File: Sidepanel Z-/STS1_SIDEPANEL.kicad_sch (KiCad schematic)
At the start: 7 parts, among them J1 Conn_01x18, J3 Conn_01x12

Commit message: moved the connectors, changed the footprint of the input and output capacitors and splitted the input capacitor in two
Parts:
- UV1: footprint STS_connector:5014610491 -> STS_connector:200528-0040
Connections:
- net at cam1.1: now also edu_con1.22; no longer edu_con1.1
- net at cam1.10: now also edu_con1.13; no longer edu_con1.10
- net at cam1.11: now also edu_con1.12; no longer edu_con1.11
- net at cam1.12: now also edu_con1.11; no longer edu_con1.12
- net at cam1.13: now also edu_con1.10; no longer edu_con1.13
- net at cam1.14: now also edu_con1.9; no longer edu_con1.14
- net at cam1.15: now also edu_con1.8; no longer edu_con1.15
- net at cam1.16: now also edu_con1.7; no longer edu_con1.16
- net at cam1.17: now also edu_con1.6; no longer edu_con1.17
- net at cam1.18: now also edu_con1.5; no longer edu_con1.18
- net at cam1.19: now also edu_con1.4; no longer edu_con1.19
- net at cam1.2: now also edu_con1.21; no longer edu_con1.2
- net at cam1.20: now also edu_con1.3; no longer edu_con1.20
- net at cam1.21: now also edu_con1.2; no longer edu_con1.21
- net at cam1.22: now also edu_con1.1; no longer edu_con1.22
- net at cam1.3: now also edu_con1.20; no longer edu_con1.3
- net at cam1.4: now also edu_con1.19; no longer edu_con1.4
- net at cam1.5: now also edu_con1.18; no longer edu_con1.5
- net at cam1.6: now also edu_con1.17; no longer edu_con1.6
- net at cam1.7: now also edu_con1.16; no longer edu_con1.7
- net at cam1.8: now also edu_con1.15; no longer edu_con1.8
- net at cam1.9: now also edu_con1.14; no longer edu_con1.9
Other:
- moved on the sheet: edu_con1
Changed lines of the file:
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@@
   (no_connect (at 132.715 71.755))
   (no_connect (at 40.64 119.38))
-  (no_connect (at 182.245 71.755))
+  (no_connect (at 182.245 122.555))
   (no_connect (at 40.005 109.22))
   (no_connect (at 79.375 78.74))
-  (no_connect (at 182.245 69.215))
+  (no_connect (at 182.245 120.015))
   (no_connect (at 132.715 69.215))
   (no_connect (at 40.005 106.68))
@@
     )
   )
-  (symbol (lib_id "Cam:54548-2271") (at 182.245 69.215 0) (mirror y) (unit 1)
-    (in_bom yes) (on_board yes) (dnp no) (fields_autoplaced)
-    (property "Reference" "edu_con1" (at 170.815 56.515 0)
+  (symbol (lib_id "Cam:54548-2271") (at 182.245 122.555 180) (unit 1)
+    (in_bom yes) (on_board yes) (dnp no)
+    (property "Reference" "edu_con1" (at 170.815 135.255 0)
       (effects (font (size 1.27 1.27)))
     )
-    (property "Value" "54548-2271" (at 170.815 59.055 0)
+    (property "Value" "54548-2271" (at 170.815 132.715 0)
       (effects (font (size 1.27 1.27)))
     )
-    (property "Footprint" "STS_connector:545482271" (at 182.245 69.215 0)
-      (effects (font (size 1.27 1.27)) hide)
-    )
-    (property "Datasheet" "" (at 182.245 69.215 0)
-      (effects (font (size 1.27 1.27)) hide)
-    )
-    (property "Reference_1" "J4" (at 170.815 61.595 0)
+    (property "Footprint" "STS_connector:545482271" (at 182.245 122.555 0)
+      (effects (font (size 1.27 1.27)) hide)
+    )
+    (property "Datasheet" "" (at 182.245 122.555 0)
+      (effects (font (size 1.27 1.27)) hide)
+    )
+    (property "Reference_1" "J4" (at 170.815 130.175 0)
       (effects (font (size 1.27 1.27)))
     )
-    (property "Value_1" "54548-2271" (at 170.815 64.135 0)
-      (effects (font (size 1.27 1.27)) hide)
-    )
-    (property "Footprint_1" "545482271" (at 163.195 164.135 0)
-      (effects (font (size 1.27 1.27)) (justify left top) hide)
-    )
-    (property "Datasheet_1" "http://www.molex.com/webdocs/datasheets/pdf/en-us//0545482271_FFC_FPC_CONNECTORS.pdf" (at 163.195 264.135 0)
-      (effects (font (size 1.27 1.27)) (justify left top) hide)
-    )
-    (property "Height" "1" (at 163.195 464.135 0)
-      (effects (font (size 1.27 1.27)) (justify left top) hide)
-    )
-    (property "Manufacturer_Name" "Molex" (at 163.195 564.135 0)
-      (effects (font (size 1.27 1.27)) (justify left top) hide)
-    )
-    (property "Manufacturer_Part_Number" "54548-2271" (at 163.195 664.135 0)
-      (effects (font (size 1.27 1.27)) (justify left top) hide)
-    )
-    (property "Mouser Part Number" "538-54548-2271" (at 163.195 764.135 0)
-      (effects (font (size 1.27 1.27)) (justify left top) hide)
-    )
-    (property "Mouser Price/Stock" "https://www.mouser.co.uk/ProductDetail/Molex/54548-2271?qs=qM7ngqbhX5X3ZiWzRWv9wA%3D%3D" (at 163.195 864.135 0)
-      (effects (font (size 1.27 1.27)) (justify left top) hide)
-    )
-    (property "Arrow Part Number" "" (at 163.195 964.135 0)
-      (effects (font (size 1.27 1.27)) (justify left top) hide)
-    )
-    (property "Arrow Price/Stock" "" (at 163.195 1064.135 0)
+    (property "Value_1" "54548-2271" (at 170.815 127.635 0)
+      (effects (font (size 1.27 1.27)) hide)
+    )
+    (property "Footprint_1" "545482271" (at 163.195 27.635 0)
+      (effects (font (size 1.27 1.27)) (justify left top) hide)
+    )
+    (property "Datasheet_1" "http://www.molex.com/webdocs/datasheets/pdf/en-us//0545482271_FFC_FPC_CONNECTORS.pdf" (at 163.195 -72.365 0)
+      (effects (font (size 1.27 1.27)) (justify left top) hide)
+    )
+    (property "Height" "1" (at 163.195 -272.365 0)
+      (effects (font (size 1.27 1.27)) (justify left top) hide)
+    )
+    (property "Manufacturer_Name" "Molex" (at 163.195 -372.365 0)
+      (effects (font (size 1.27 1.27)) (justify left top) hide)
+    )
+    (property "Manufacturer_Part_Number" "54548-2271" (at 163.195 -472.365 0)
+      (effects (font (size 1.27 1.27)) (justify left top) hide)
+    )
+    (property "Mouser Part Number" "538-54548-2271" (at 163.195 -572.365 0)
+      (effects (font (size 1.27 1.27)) (justify left top) hide)
+    )
+    (property "Mouser Price/Stock" "https://www.mouser.co.uk/ProductDetail/Molex/54548-2271?qs=qM7ngqbhX5X3ZiWzRWv9wA%3D%3D" (at 163.195 -672.365 0)
+      (effects (font (size 1.27 1.27)) (justify left top) hide)
+    )
+    (property "Arrow Part Number" "" (at 163.195 -772.365 0)
+      (effects (font (size 1.27 1.27)) (justify left top) hide)
+    )
+    (property "Arrow Price/Stock" "" (at 163.195 -872.365 0)
       (effects (font (size 1.27 1.27)) (justify left top) hide)
     )
@@
       (effects (font (size 1.27 1.27)) hide)
     )
-    (property "Footprint" "STS_connector:5014610491" (at 79.375 76.2 0)
-      (effects (font (size 1.27 1.27)) hide)
-    )
+    (property "Footprint" "STS_connector:200528-0040" (at 79.375 76.2 0)
+      (effects (font (size 1.27 1.27)) hide)
+    )

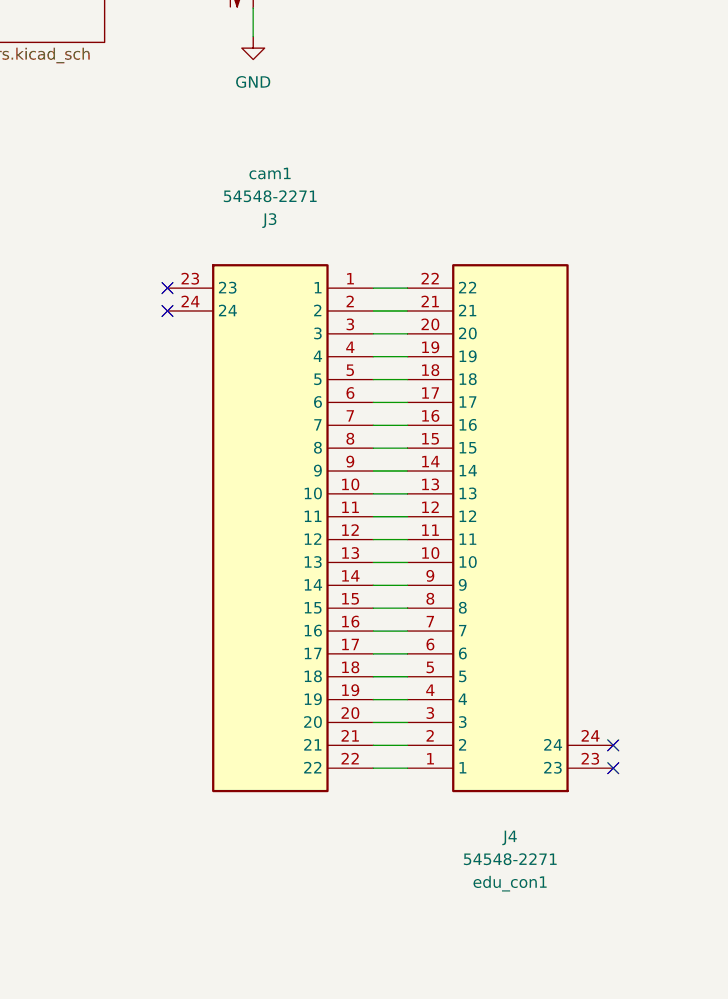
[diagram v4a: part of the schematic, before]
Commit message: Z- Cam Connerctor Rerout, add vias & 90deg trace removal
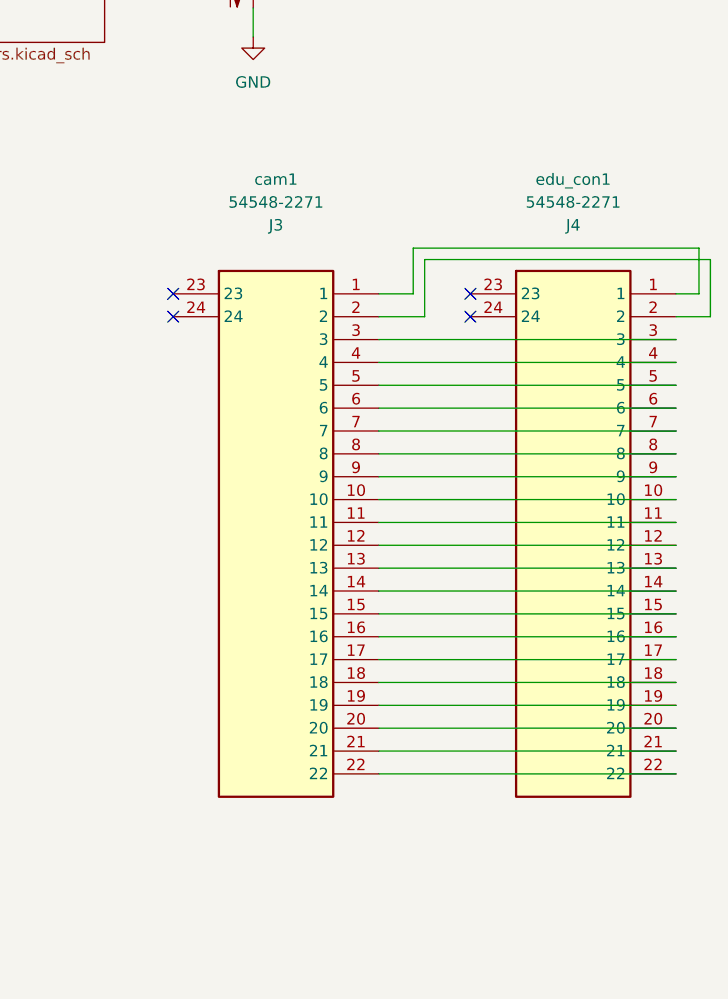
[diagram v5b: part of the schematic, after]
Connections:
- net at cam1.1: now also edu_con1.1; no longer edu_con1.22
- net at cam1.10: now also edu_con1.10; no longer edu_con1.13
- net at cam1.11: now also edu_con1.11; no longer edu_con1.12
- net at cam1.12: now also edu_con1.12; no longer edu_con1.11
- net at cam1.13: now also edu_con1.13; no longer edu_con1.10
- net at cam1.14: now also edu_con1.14; no longer edu_con1.9
- net at cam1.15: now also edu_con1.15; no longer edu_con1.8
- net at cam1.16: now also edu_con1.16; no longer edu_con1.7
- net at cam1.17: now also edu_con1.17; no longer edu_con1.6
- net at cam1.18: now also edu_con1.18; no longer edu_con1.5
- net at cam1.19: now also edu_con1.19; no longer edu_con1.4
- net at cam1.2: now also edu_con1.2; no longer edu_con1.21
- net at cam1.20: now also edu_con1.20; no longer edu_con1.3
- net at cam1.21: now also edu_con1.21; no longer edu_con1.2
- net at cam1.22: now also edu_con1.22; no longer edu_con1.1
- net at cam1.3: now also edu_con1.3; no longer edu_con1.20
- net at cam1.4: now also edu_con1.4; no longer edu_con1.19
- net at cam1.5: now also edu_con1.5; no longer edu_con1.18
- net at cam1.6: now also edu_con1.6; no longer edu_con1.17
- net at cam1.7: now also edu_con1.7; no longer edu_con1.16
- net at cam1.8: now also edu_con1.8; no longer edu_con1.15
- net at cam1.9: now also edu_con1.9; no longer edu_con1.14
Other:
- moved on the sheet: cam1, edu_con1

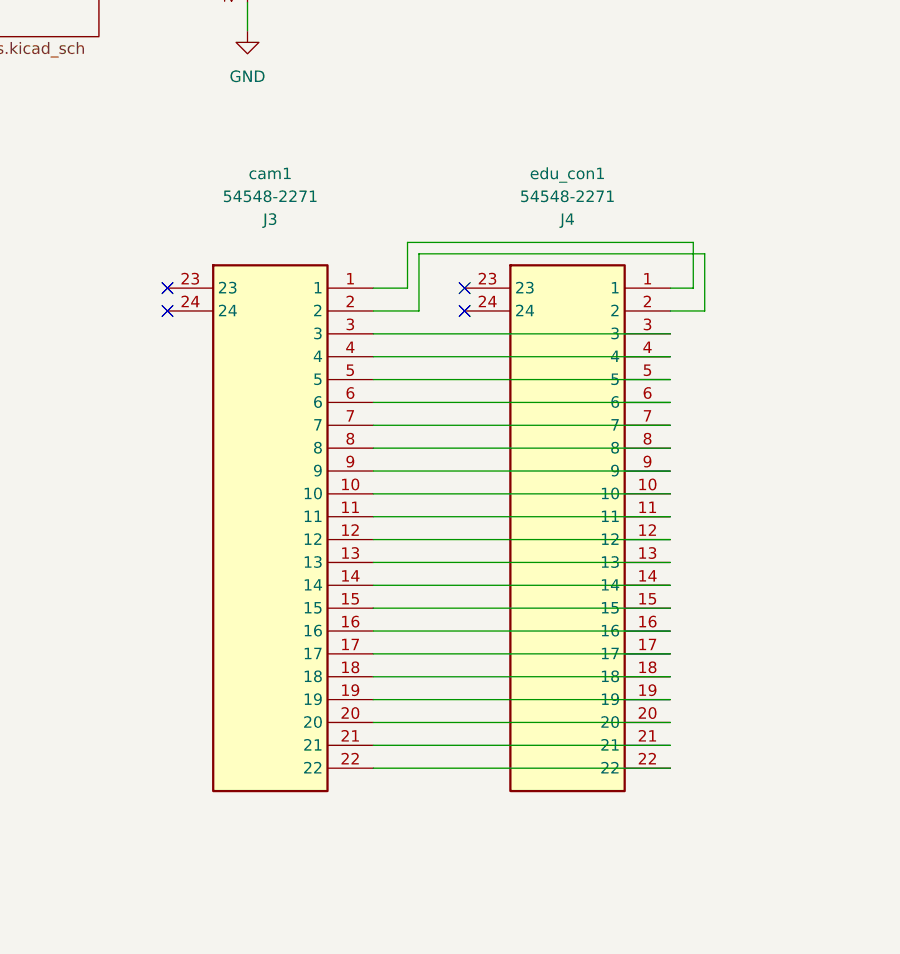
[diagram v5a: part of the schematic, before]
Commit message: chaned the connectors for the cameras from buttom to top contact
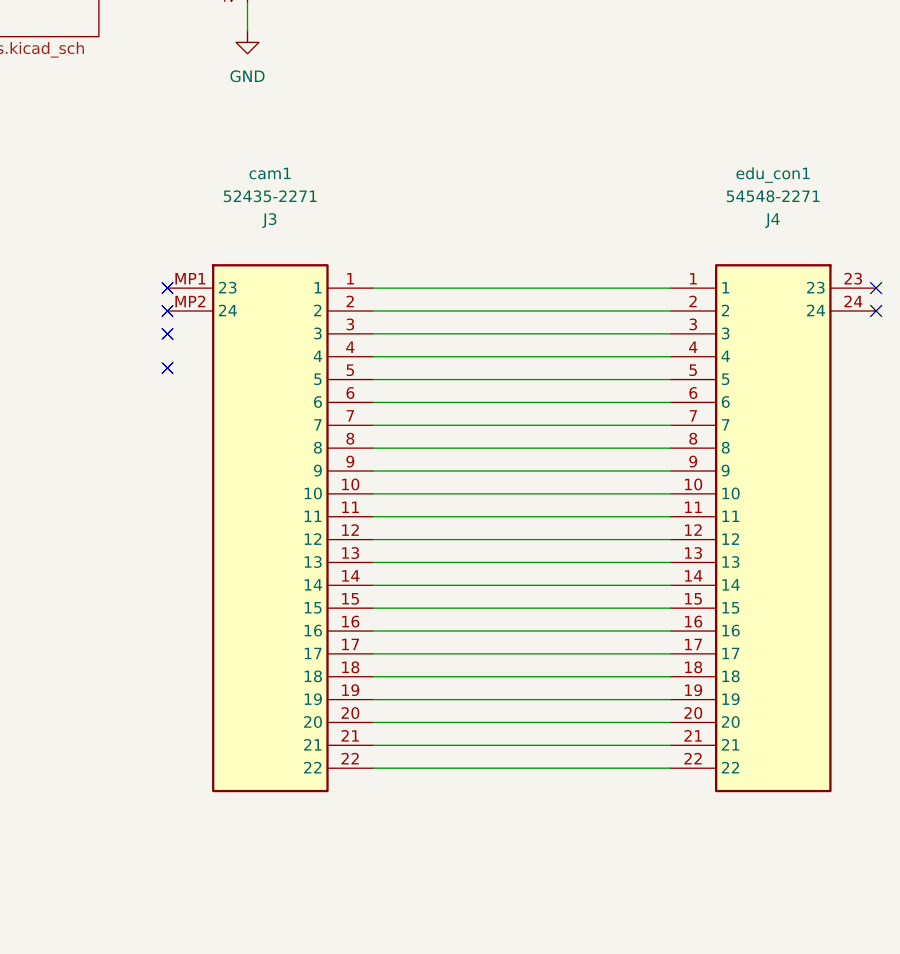
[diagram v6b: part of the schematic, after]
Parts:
- cam1: value 54548-2271 -> 52435-2271; footprint STS_connector:545482271 -> STS_connector:524352271
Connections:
- no-connect marks 11 -> 13
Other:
- moved on the sheet: edu_con1
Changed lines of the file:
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@@
 	(paper "A4")
 	(no_connect
+		(at 133.35 78.74)
+	)
+	(no_connect
 		(at 40.64 116.84)
 	)
@@
 	)
 	(no_connect
-		(at 166.37 69.85)
+		(at 133.35 74.93)
+	)
+	(no_connect
+		(at 212.09 69.85)
 	)
 	(no_connect
@@
 	)
 	(no_connect
-		(at 166.37 72.39)
+		(at 212.09 72.39)
 	)
 	(no_connect
@@
 	(wire
 		(pts
+			(xy 156.21 69.85) (xy 189.23 69.85)
+		)
+		(stroke
+			(width 0)
+			(type default)
+		)
+	)
+	(wire
+		(pts
 			(xy 142.24 38.1) (xy 142.24 41.275)
 		)
@@
 	(wire
 		(pts
-			(xy 191.77 69.85) (xy 189.23 69.85)
-		)
-		(stroke
-			(width 0)
-			(type default)
-		)
-	)
-	(wire
-		(pts
 			(xy 96.52 36.83) (xy 104.14 36.83)
 		)
@@
 	(wire
 		(pts
-			(xy 160.02 64.77) (xy 191.77 64.77)
-		)
-		(stroke
-			(width 0)
-			(type default)
-		)
-	)
-	(wire
-		(pts
-			(xy 189.23 72.39) (xy 193.04 72.39)
-		)
-		(stroke
-			(width 0)
-			(type default)
-		)
-	)
-	(wire
-		(pts
-			(xy 156.21 69.85) (xy 160.02 69.85)
-		)
-		(stroke
-			(width 0)
-			(type default)
-		)
-	)
-	(wire
-		(pts
 			(xy 72.39 34.29) (xy 82.55 34.29)
 		)
@@
 	(wire
 		(pts
-			(xy 193.04 72.39) (xy 193.04 66.04)
+			(xy 156.21 72.39) (xy 189.23 72.39)
 		)
 		(stroke
@@
 	(wire
 		(pts
-			(xy 191.77 64.77) (xy 191.77 69.85)
-		)
-		(stroke
-			(width 0)
-			(type default)
-		)
-	)
-	(wire
-		(pts
 			(xy 96.52 34.29) (xy 104.14 34.29)
 		)
@@
 	(wire
 		(pts
-			(xy 161.29 72.39) (xy 156.21 72.39)
-		)
-		(stroke
-			(width 0)
-			(type default)
-		)
-	)
-	(wire
-		(pts
 			(xy 156.21 80.01) (xy 189.23 80.01)
 		)
@@
 	(wire
 		(pts
-			(xy 161.29 66.04) (xy 161.29 72.39)
-		)
-		(stroke
-			(width 0)
-			(type default)
-		)
-	)
-	(wire
-		(pts
 			(xy 156.21 107.95) (xy 189.23 107.95)
 		)
@@
 		(pts
 			(xy 29.845 73.66) (xy 40.005 73.66)
-		)
-		(stroke
-			(width 0)
-			(type default)
-		)
-	)
-	(wire
-		(pts
-			(xy 193.04 66.04) (xy 161.29 66.04)
-		)
-		(stroke
-			(width 0)
-			(type default)
-		)
-	)
-	(wire
-		(pts
-			(xy 160.02 69.85) (xy 160.02 64.77)
 		)
 		(stroke
@@
 	)
 	(symbol
+		(lib_name "54548-2271_1")
 		(lib_id "Cam:54548-2271")
 		(at 133.35 69.85 0)
@@
 			)
 		)
-		(property "Value" "54548-2271"
+		(property "Value" "52435-2271"
 			(at 144.78 59.69 0)
 			(effects
@@
 			)
 		)
-		(property "Footprint" "STS_connector:545482271"
-			(at 133.35 69.85 0)
+		(property "Footprint" "STS_connector:524352271"
+			(at 124.714 62.738 0)
 			(effects
 				(font
@@
 		(pin "22"
 		)
-		(pin "23"
-		)
-		(pin "24"
+		(pin "MP1"
+		)
+		(pin "MP2"
 		)
 		(pin "3"
@@
 	(symbol
 		(lib_id "Cam:54548-2271")
-		(at 166.37 69.85 0)
+		(at 212.09 69.85 0)
+		(mirror y)
 		(unit 1)
 		(exclude_from_sim no)
@@
 		(dnp no)
 		(property "Reference" "edu_con1"
-			(at 177.8 57.15 0)
+			(at 200.66 57.15 0)
 			(effects
 				(font
@@
 		)
 		(property "Value" "54548-2271"
-			(at 177.8 59.69 0)
+			(at 200.66 59.69 0)
 			(effects
 				(font
@@
 		)
 		(property "Footprint" "STS_connector:545482271"
-			(at 166.37 69.85 0)
+			(at 212.09 69.85 0)
 			(effects
 				(font
@@
 		)
 		(property "Datasheet" ""
-			(at 166.37 69.85 0)
+			(at 212.09 69.85 0)
 			(effects
 				(font
@@
 		)
 		(property "Description" ""
-			(at 166.37 69.85 0)
+			(at 212.09 69.85 0)
 			(effects
 				(font
@@
 		)
 		(property "Reference_1" "J4"
-			(at 177.8 62.23 0)
+			(at 200.66 62.23 0)
 			(effects
 				(font
@@
 		)
 		(property "Value_1" "54548-2271"
-			(at 177.8 64.77 0)
+			(at 200.66 64.77 0)
 			(effects
 				(font
@@
 		)
 		(property "Footprint_1" "545482271"
-			(at 185.42 164.77 0)
+			(at 193.04 164.77 0)
 			(effects
 				(font
@@
 		)
 		(property "Datasheet_1" "http://www.molex.com/webdocs/datasheets/pdf/en-us//0545482271_FFC_FPC_CONNECTORS.pdf"
-			(at 185.42 264.77 0)
+			(at 193.04 264.77 0)
 			(effects
 				(font
@@
 		)
 		(property "Height" "1"
-			(at 185.42 464.77 0)
+			(at 193.04 464.77 0)
 			(effects
 				(font
@@
 		)
 		(property "Manufacturer_Name" "Molex"
-			(at 185.42 564.77 0)
+			(at 193.04 564.77 0)
 			(effects
 				(font
@@
 		)
 		(property "Manufacturer_Part_Number" "54548-2271"
-			(at 185.42 664.77 0)
+			(at 193.04 664.77 0)
 			(effects
 				(font
@@
 		)
 		(property "Mouser Part Number" "538-54548-2271"
-			(at 185.42 764.77 0)
+			(at 193.04 764.77 0)
 			(effects
 				(font
@@
 		)
 		(property "Mouser Price/Stock" "https://www.mouser.co.uk/ProductDetail/Molex/54548-2271?qs=qM7ngqbhX5X3ZiWzRWv9wA%3D%3D"
-			(at 185.42 864.77 0)
+			(at 193.04 864.77 0)
 			(effects
 				(font
@@
 		)
 		(property "Arrow Part Number" ""
-			(at 185.42 964.77 0)
+			(at 193.04 964.77 0)
 			(effects
 				(font
@@
 		)
 		(property "Arrow Price/Stock" ""
-			(at 185.42 1064.77 0)
-			(effects
-				(font
+			(at 193.04 1064.77 0)
+			(effects
+				(font
